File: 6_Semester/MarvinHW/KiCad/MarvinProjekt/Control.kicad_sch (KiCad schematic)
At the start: 9 parts, among them SW3 SW_DPST_x2, SW4 SW_DPST_x2, SW5 SW_DPST_x2, SW6 SW_DPST_x2

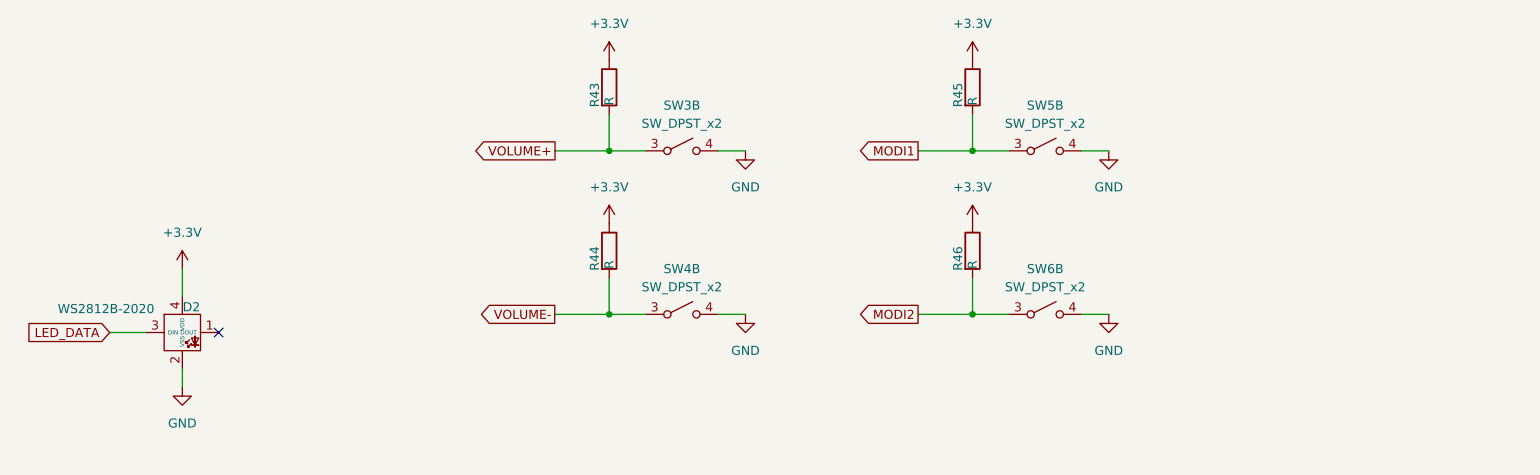
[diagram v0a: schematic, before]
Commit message: renamed untitledsheet to crontrol
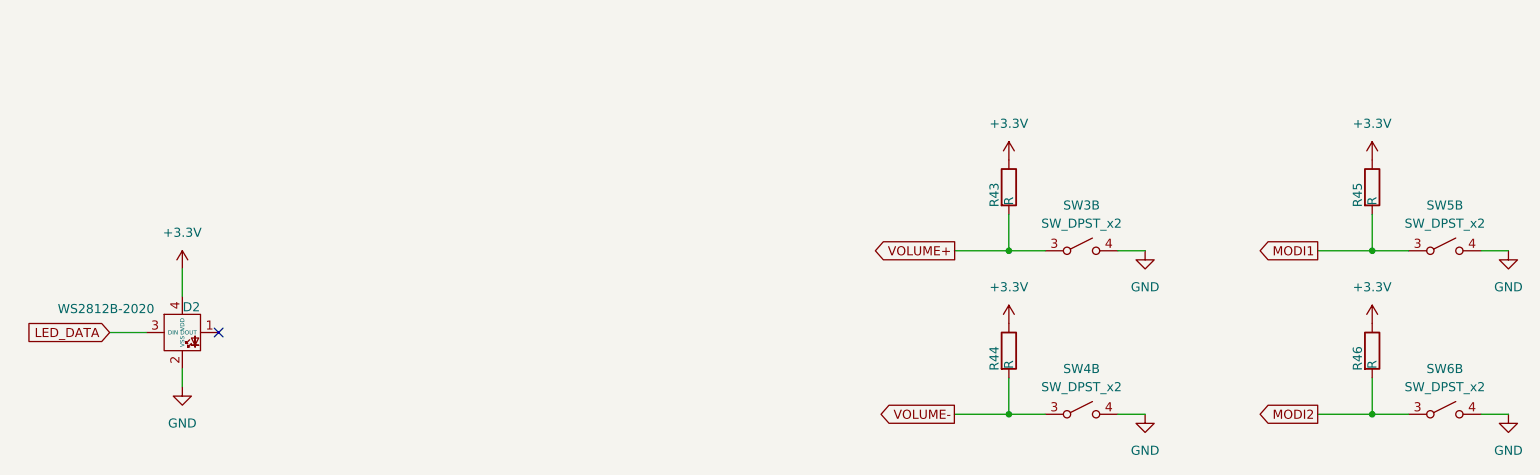
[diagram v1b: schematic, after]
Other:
- moved on the sheet: R43, R44, R45, R46, SW3B, SW4B, SW5B, SW6B

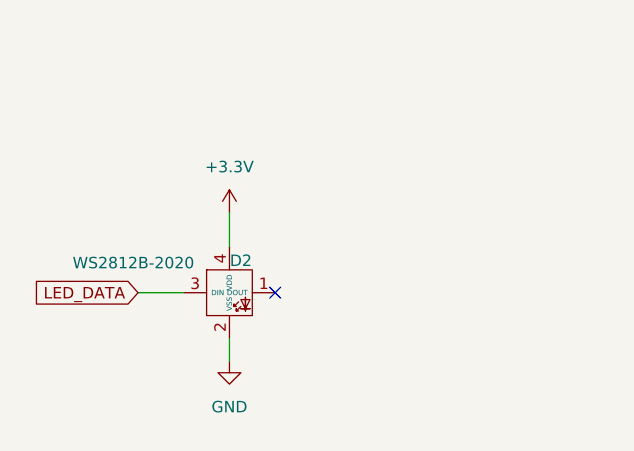
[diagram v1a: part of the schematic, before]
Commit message: finished schematic working on footprints
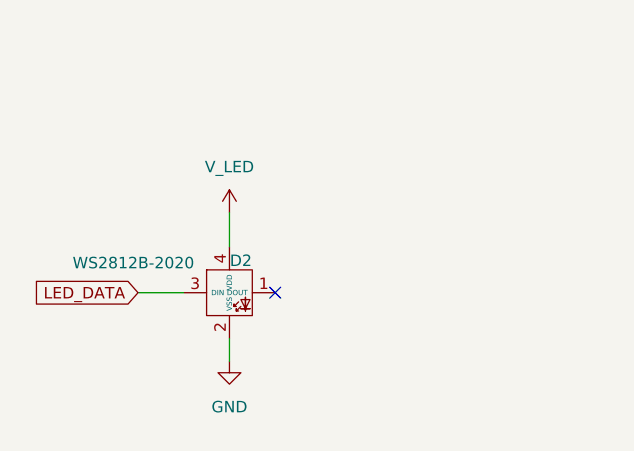
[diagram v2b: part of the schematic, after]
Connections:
- net +3.3V: no longer D2.4 (VDD)
- new net V_LED: D2.4 (VDD)
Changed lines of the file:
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@@
 			)
 		)
-		(property "Value" "+3.3V"
+		(property "Value" "V_LED"
 			(at 57.15 49.53 0)
 			(effects
